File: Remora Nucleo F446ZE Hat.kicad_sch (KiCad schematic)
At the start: 20 parts, among them J1 NucleoF446ZE CN11 Header, J2 NucleoF446ZE CN12 Header, J3 UART_TX, J4 MSD-1-A, SW2 SW_Push

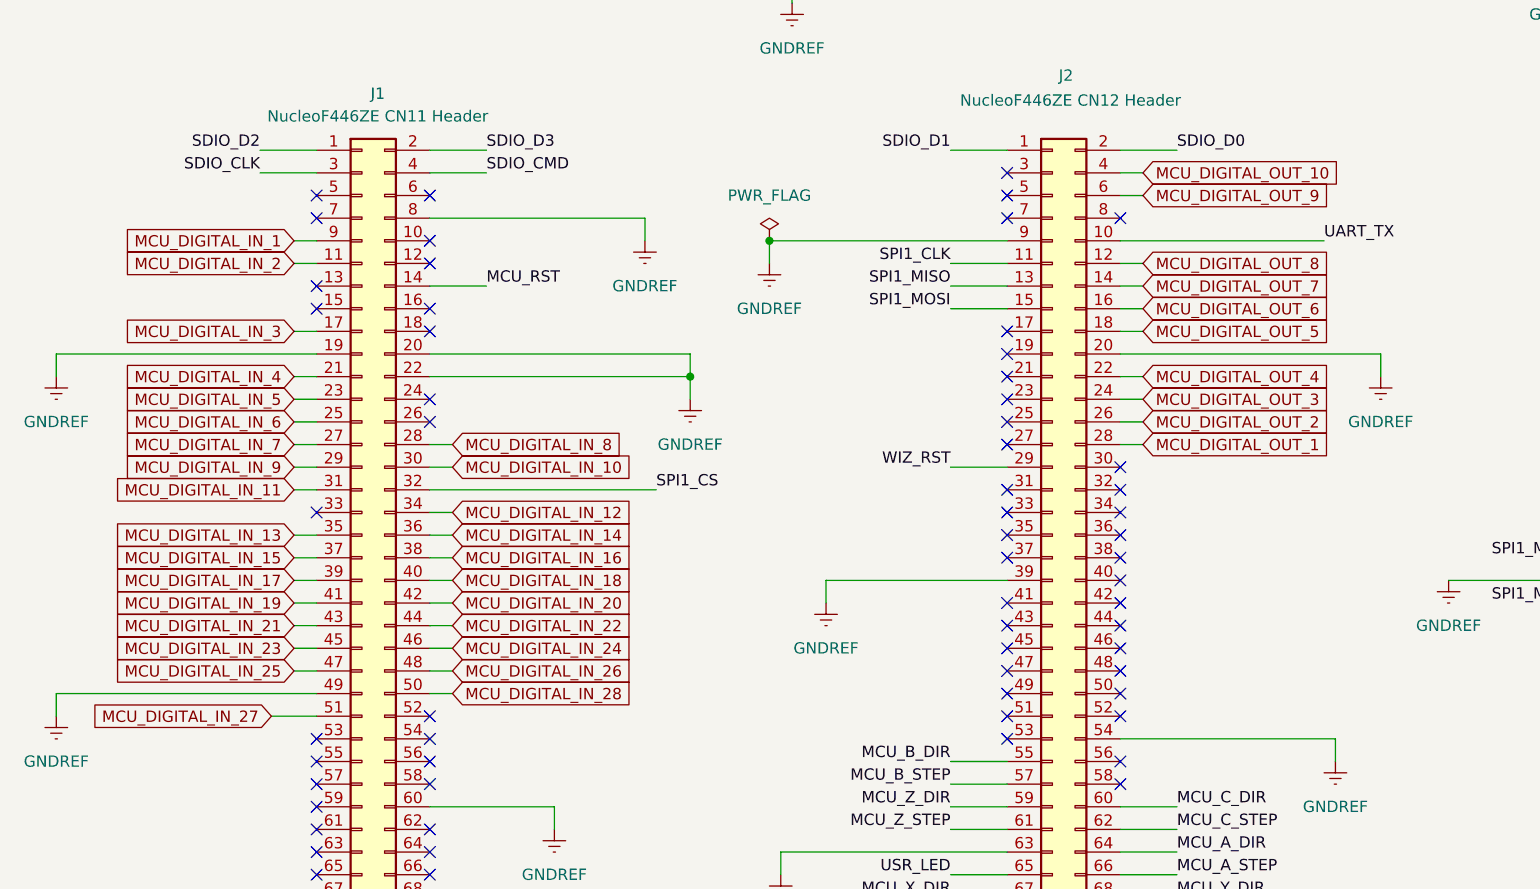
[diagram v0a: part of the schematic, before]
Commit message: Dropped number of IO on design to make more room. Created the new footprints to suit them, updates to BOM and ran some traces on the PCB.
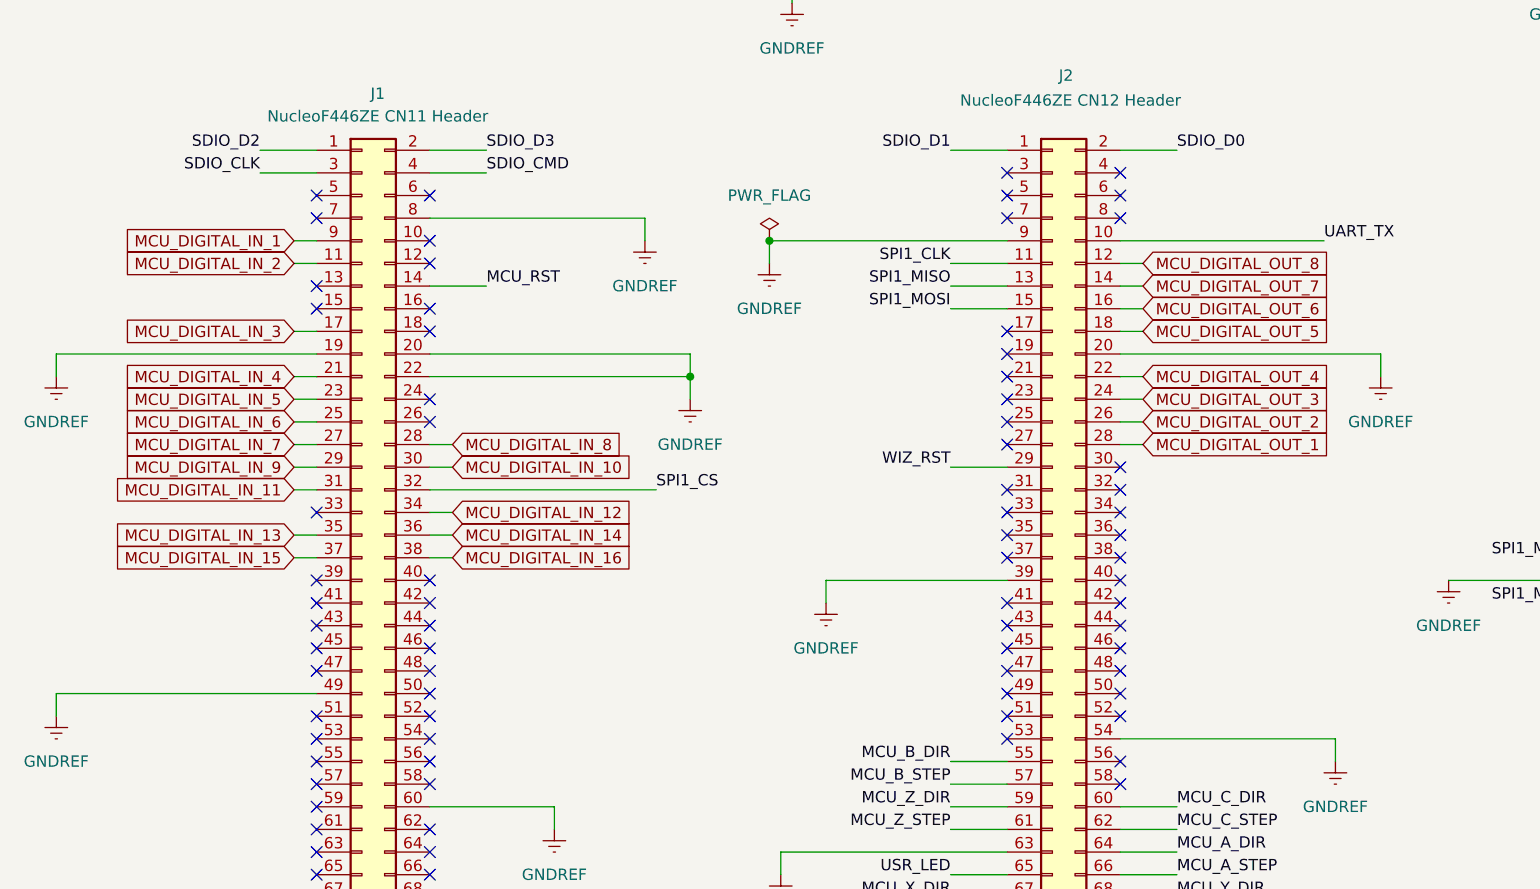
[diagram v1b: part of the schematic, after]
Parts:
- RP1: footprint RASPBERRYPI -> RPI3FootPrint:raspberrypi_2_3
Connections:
- net MCU_DIGITAL_IN_17: no longer names the net of J1.39 (Pin_39)
- net MCU_DIGITAL_IN_18: no longer names the net of J1.40 (Pin_40)
- net MCU_DIGITAL_IN_19: no longer names the net of J1.41 (Pin_41)
- net MCU_DIGITAL_IN_20: no longer names the net of J1.42 (Pin_42)
- net MCU_DIGITAL_IN_21: no longer names the net of J1.43 (Pin_43)
- net MCU_DIGITAL_IN_22: no longer names the net of J1.44 (Pin_44)
- net MCU_DIGITAL_IN_23: no longer names the net of J1.45 (Pin_45)
- net MCU_DIGITAL_IN_24: no longer names the net of J1.46 (Pin_46)
- net MCU_DIGITAL_IN_25: no longer names the net of J1.47 (Pin_47)
- net MCU_DIGITAL_IN_26: no longer names the net of J1.48 (Pin_48)
- net MCU_DIGITAL_IN_27: no longer names the net of J1.51 (Pin_51)
- net MCU_DIGITAL_IN_28: no longer names the net of J1.50 (Pin_50)
- net MCU_DIGITAL_OUT_10: no longer names the net of J2.4 (Pin_4)
- net MCU_DIGITAL_OUT_9: no longer names the net of J2.6 (Pin_6)
- no-connect marks 99 -> 113

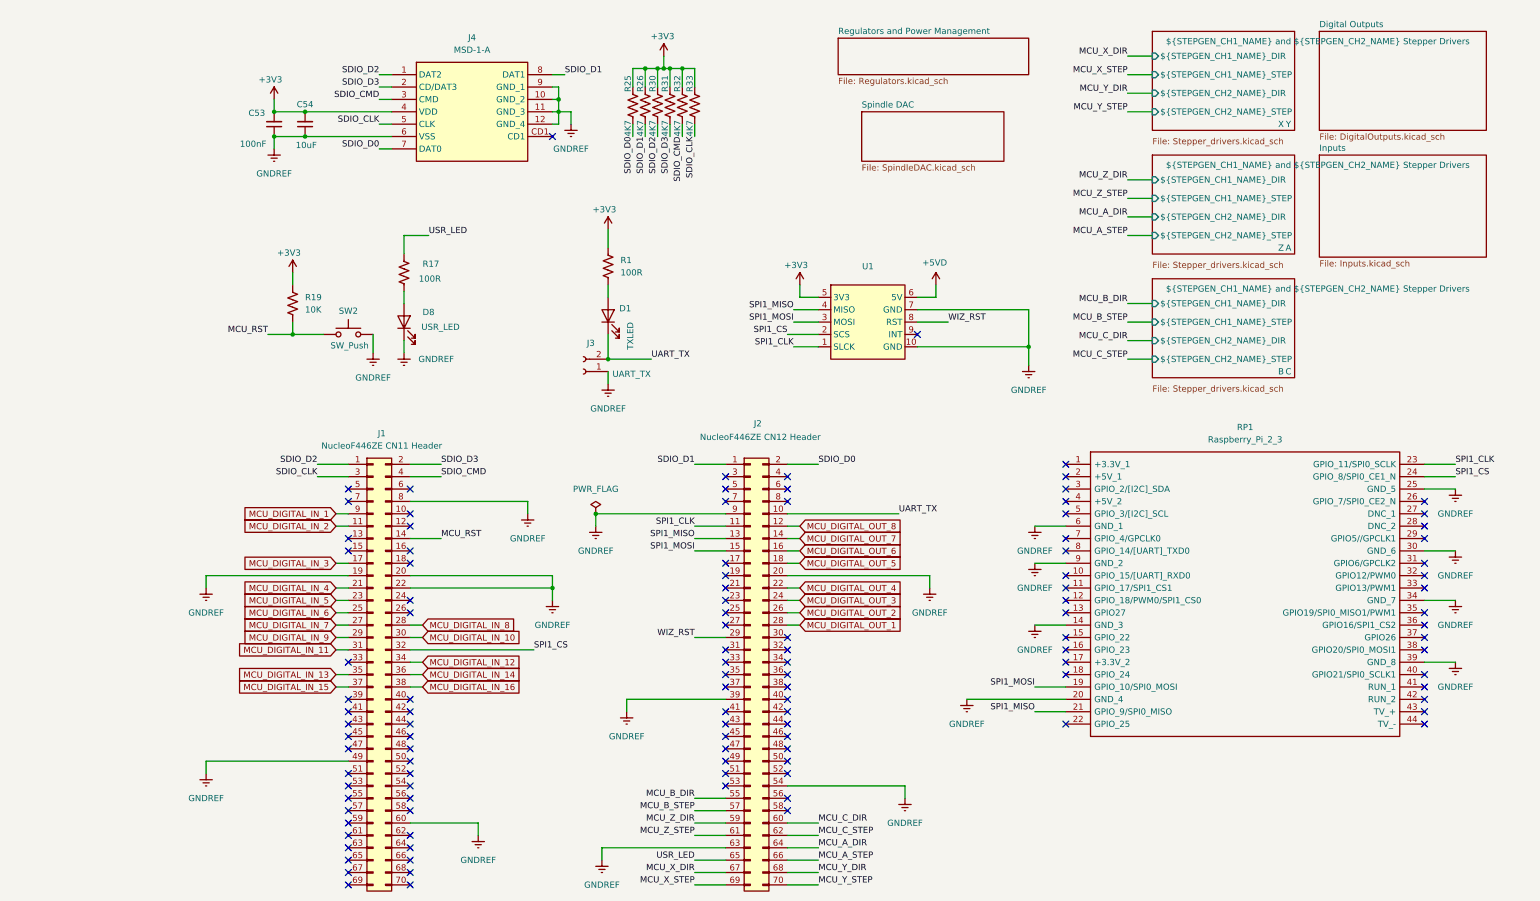
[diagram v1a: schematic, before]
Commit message: New optocoupler part choice, removed digikey BOM as have started inputting them into symbol fields. Re-enabled all disabled parts for now and will re-design power supplies soon.
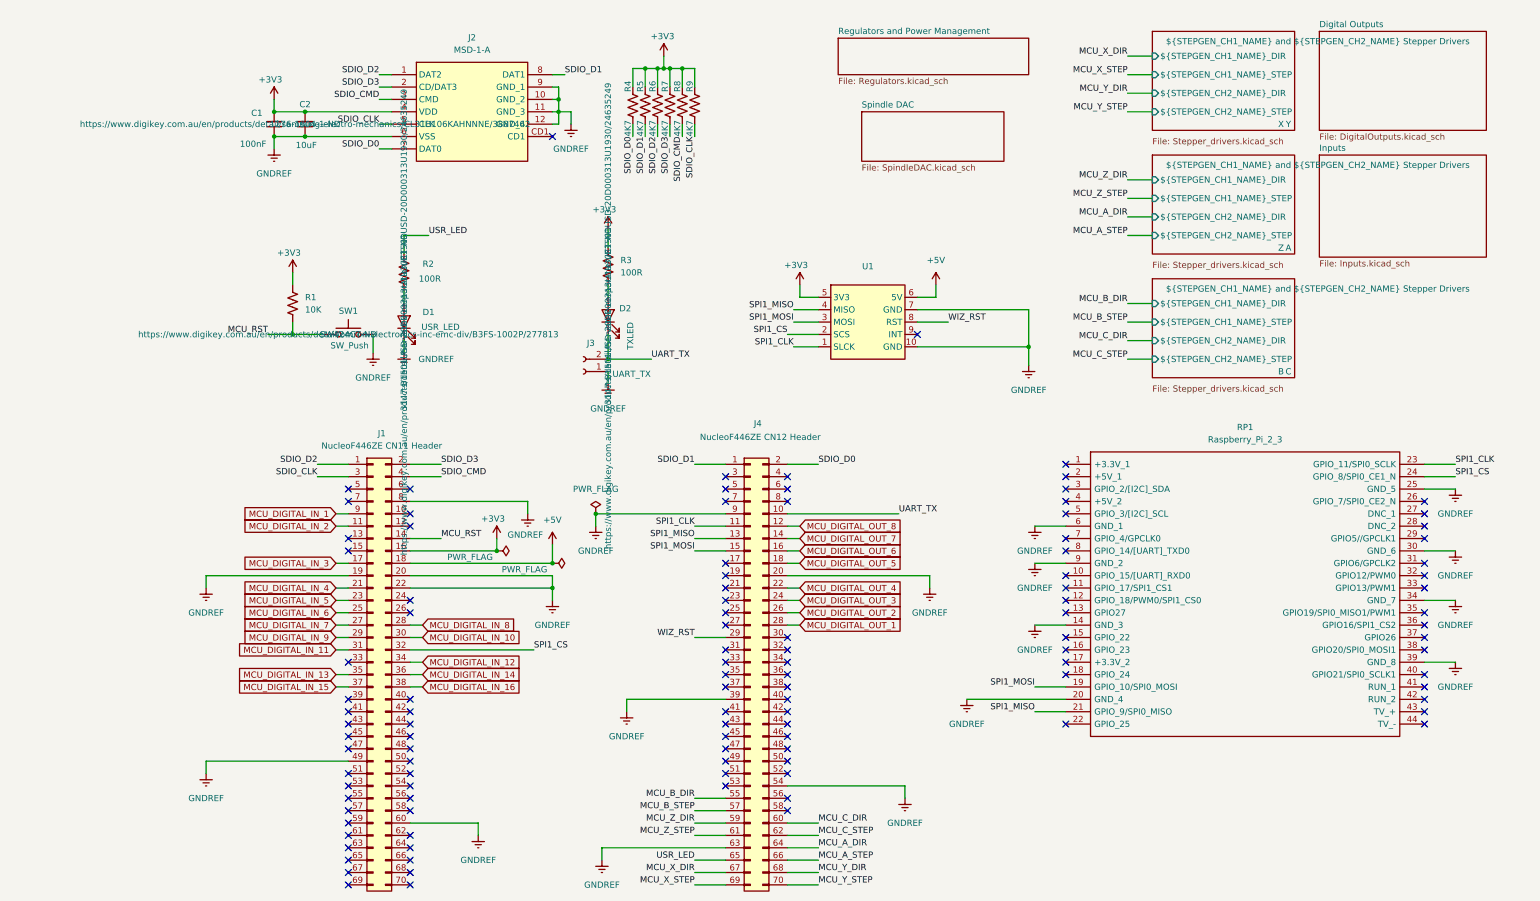
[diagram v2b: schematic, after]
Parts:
- C1: renamed from C53; Digikey Part Number (none) -> 399-C1206C104K5RACTUCT-ND; Digikey URL (none) -> https://www.digikey.com.au/en/products/detail/kemet/C1206C1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
- C2: renamed from C54; Digikey Part Number (none) -> 1276-1804-1-ND; Digikey URL (none) -> https://www.digikey.com.au/en/products/detail/samsung-elect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
- D1: renamed from D8; Digikey Part Number (none) -> 3147-B1501USD-20D000313U1930CT-ND; Digikey URL (none) -> https://www.digikey.com.au/en/products/detail/harvatek-corp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
- D2: renamed from D1; Digikey Part Number (none) -> 3147-B1501USD-20D000313U1930CT-ND; Digikey URL (none) -> https://www.digikey.com.au/en/products/detail/harvatek-corp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
- SW1: renamed from SW2; Digikey Part Number (none) -> SW424CT-ND; Digikey URL (none) -> https://www.digikey.com.au/en/products/detail/omron-electro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
- renumbered J4 to J2, J2 to J4, R19 to R1, R17 to R2, R1 to R3, R25 to R4, R26 to R5, R30 to R6, R31 to R7, R32 to R8, R33 to R9
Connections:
- net +5VD is gone; now on net +5V: U1.6 (5V)
- net +3V3: now also J1.16 (Pin_16)
- net +5V: now reaches J1.18 (Pin_18)
- no-connect marks 113 -> 111
